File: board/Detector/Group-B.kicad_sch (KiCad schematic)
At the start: 27 parts, among them J2 Conn_02x04_Odd_Even, Q5 Q_Photo_NPN, Q6 Q_Photo_NPN, Q7 Q_Photo_NPN, Q8 Q_Photo_NPN, U2 LM339

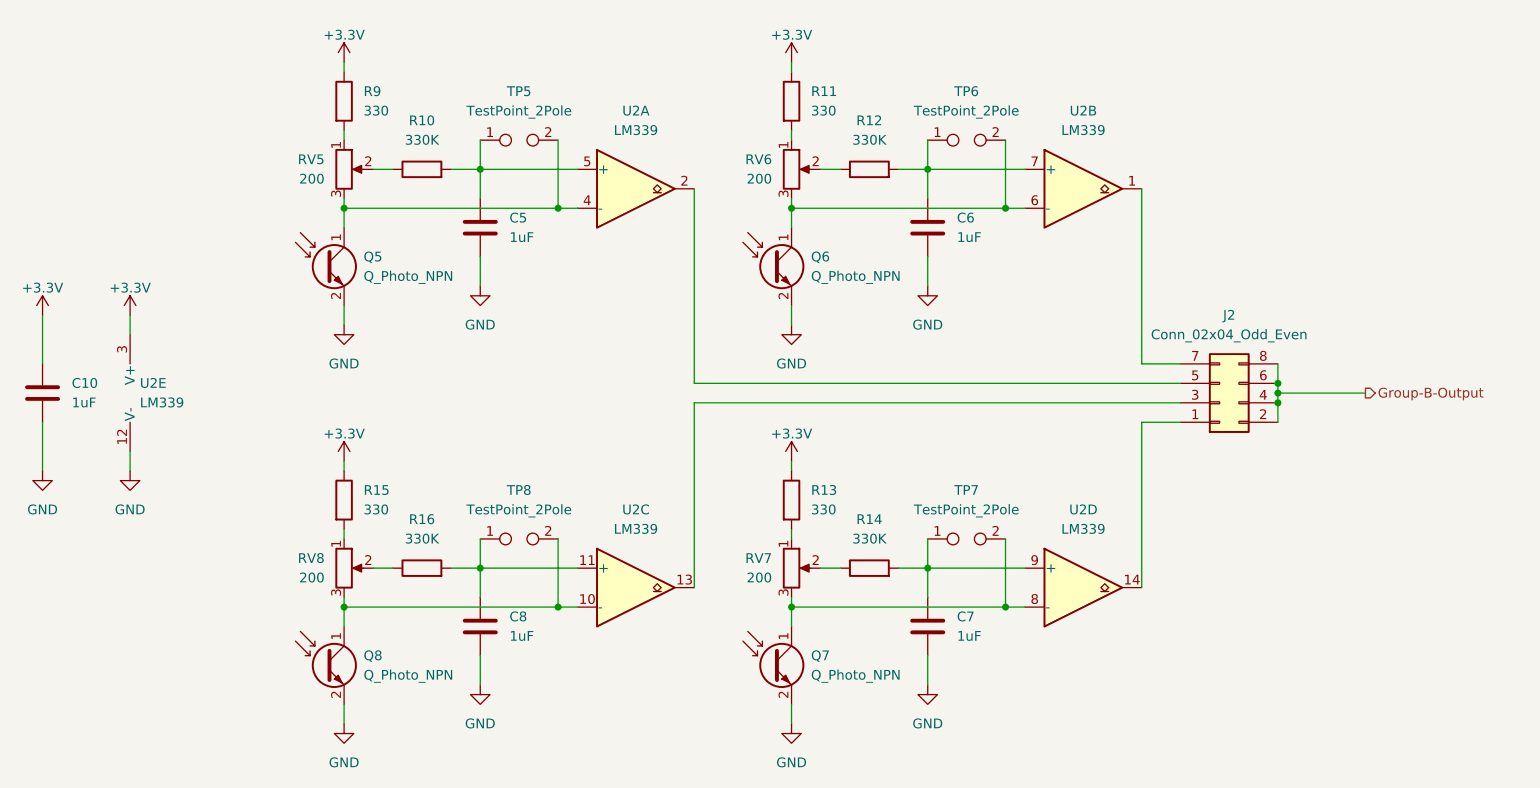
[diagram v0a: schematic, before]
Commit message: Fix the order of jumper links
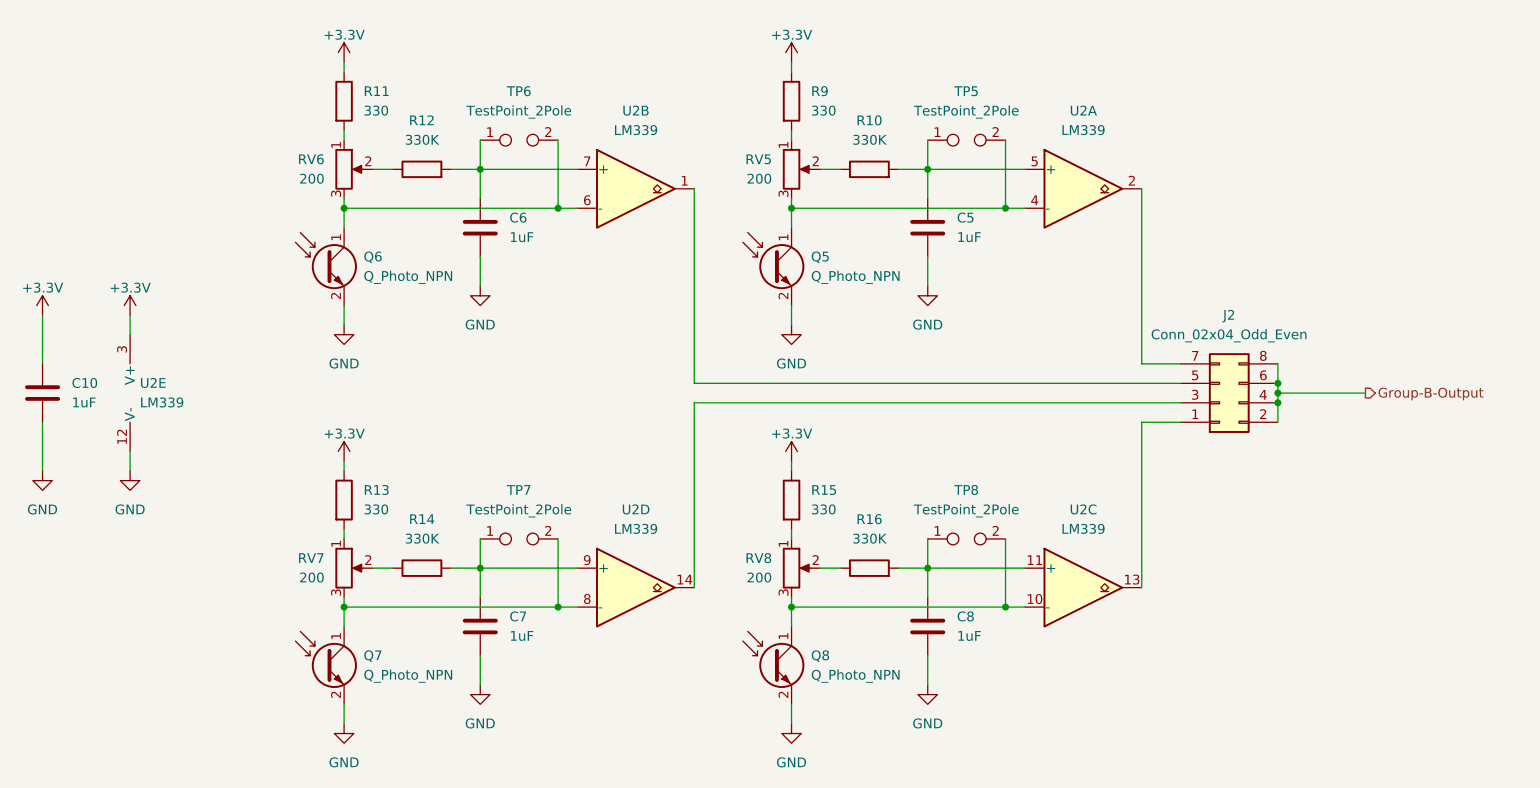
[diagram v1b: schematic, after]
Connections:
- net at U2.14: now also J2.3 (Pin_3); no longer J2.1 (Pin_1)
- net at U2.2: now also J2.7 (Pin_7); no longer J2.5 (Pin_5)
- net at U2.13: now also J2.1 (Pin_1); no longer J2.3 (Pin_3)
- net at U2.1: now also J2.5 (Pin_5); no longer J2.7 (Pin_7)
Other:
- moved on the sheet: C5, C6, C7, C8, Q5, Q6, Q7, Q8, R10, R11, R12, R13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

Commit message: Adjust values
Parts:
- Q5, Q6, Q7, Q8: value Q_Photo_NPN -> SFH 314 FA-2/3
- R11, R13, R15, R9: value 330 -> 2K
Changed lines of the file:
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@@
       (effects (font (size 1.27 1.27)) (justify left))
     )
-    (property "Value" "330" (id 1) (at 91.44 50.7999 0)
+    (property "Value" "2K" (id 1) (at 91.44 50.7999 0)
       (effects (font (size 1.27 1.27)) (justify left))
     )
@@
       (effects (font (size 1.27 1.27)) (justify left))
     )
-    (property "Value" "330" (id 1) (at 91.44 102.8699 0)
+    (property "Value" "2K" (id 1) (at 91.44 102.8699 0)
       (effects (font (size 1.27 1.27)) (justify left))
     )
@@
       (effects (font (size 1.27 1.27)) (justify left))
     )
-    (property "Value" "330" (id 1) (at 149.86 50.7999 0)
+    (property "Value" "2K" (id 1) (at 149.86 50.7999 0)
       (effects (font (size 1.27 1.27)) (justify left))
     )
@@
       (effects (font (size 1.27 1.27)) (justify left))
     )
-    (property "Value" "330" (id 1) (at 149.86 102.8699 0)
+    (property "Value" "2K" (id 1) (at 149.86 102.8699 0)
       (effects (font (size 1.27 1.27)) (justify left))
     )
@@
       (effects (font (size 1.27 1.27)) (justify left))
     )
-    (property "Value" "Q_Photo_NPN" (id 1) (at 91.44 72.3899 0)
+    (property "Value" "SFH 314 FA-2/3" (id 1) (at 91.44 72.3899 0)
       (effects (font (size 1.27 1.27)) (justify left))
     )
@@
       (effects (font (size 1.27 1.27)) (justify left))
     )
-    (property "Value" "Q_Photo_NPN" (id 1) (at 91.44 124.4599 0)
+    (property "Value" "SFH 314 FA-2/3" (id 1) (at 91.44 124.4599 0)
       (effects (font (size 1.27 1.27)) (justify left))
     )
@@
       (effects (font (size 1.27 1.27)) (justify left))
     )
-    (property "Value" "Q_Photo_NPN" (id 1) (at 149.86 72.3899 0)
+    (property "Value" "SFH 314 FA-2/3" (id 1) (at 149.86 72.3899 0)
       (effects (font (size 1.27 1.27)) (justify left))
     )
@@
       (effects (font (size 1.27 1.27)) (justify left))
     )
-    (property "Value" "Q_Photo_NPN" (id 1) (at 149.86 124.4599 0)
-      (effects (font (size 1.27 1.27)) (justify left))
-    )
+    (property "Value" "SFH 314 FA-2/3" (id 1) (at 149.86 124.4599 0)
+      (effects (font (size 1.27 1.27)) (justify left))
+    )

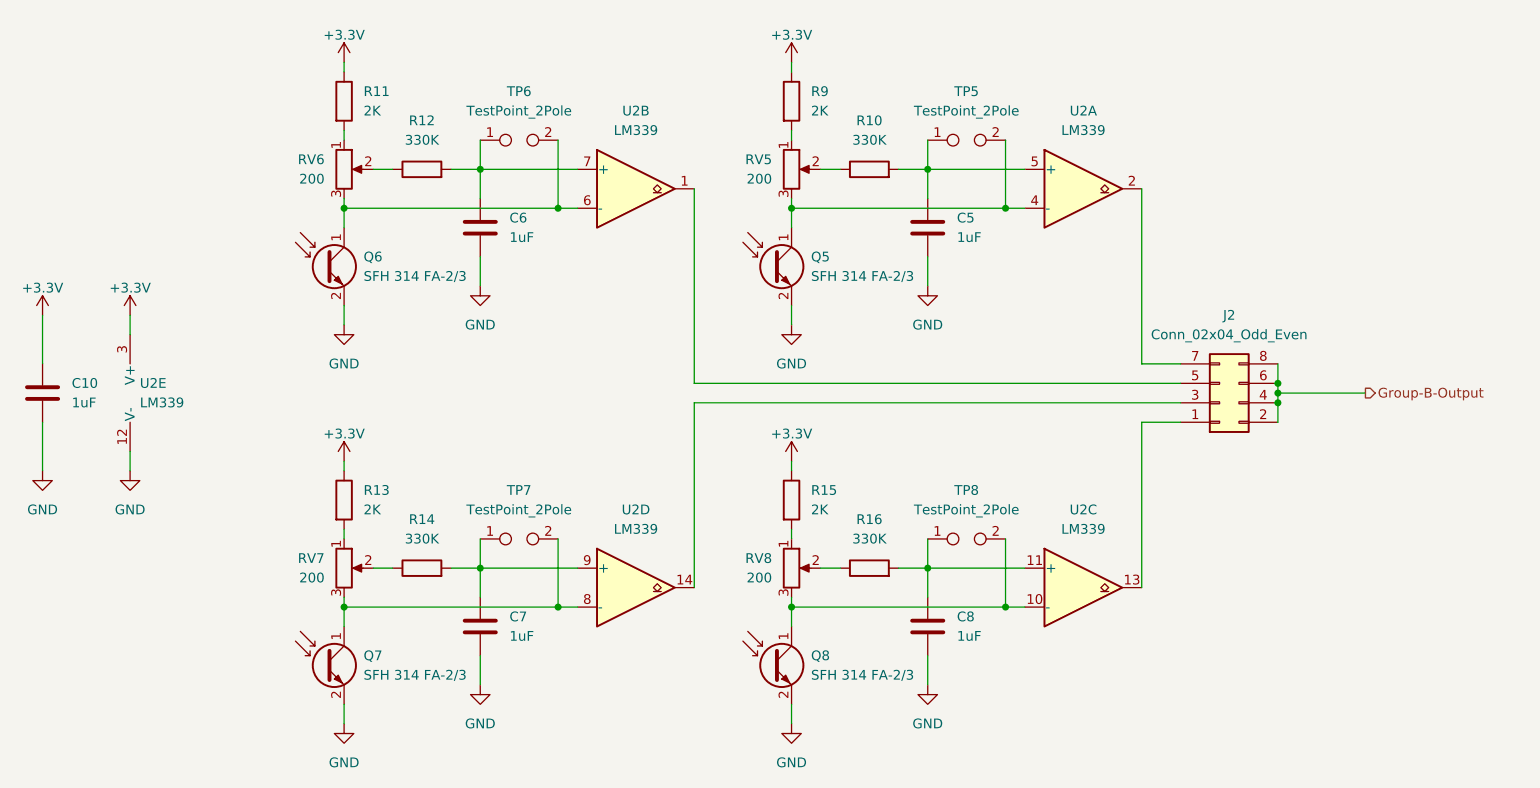
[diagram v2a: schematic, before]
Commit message: Detector changes to better control overall bias level
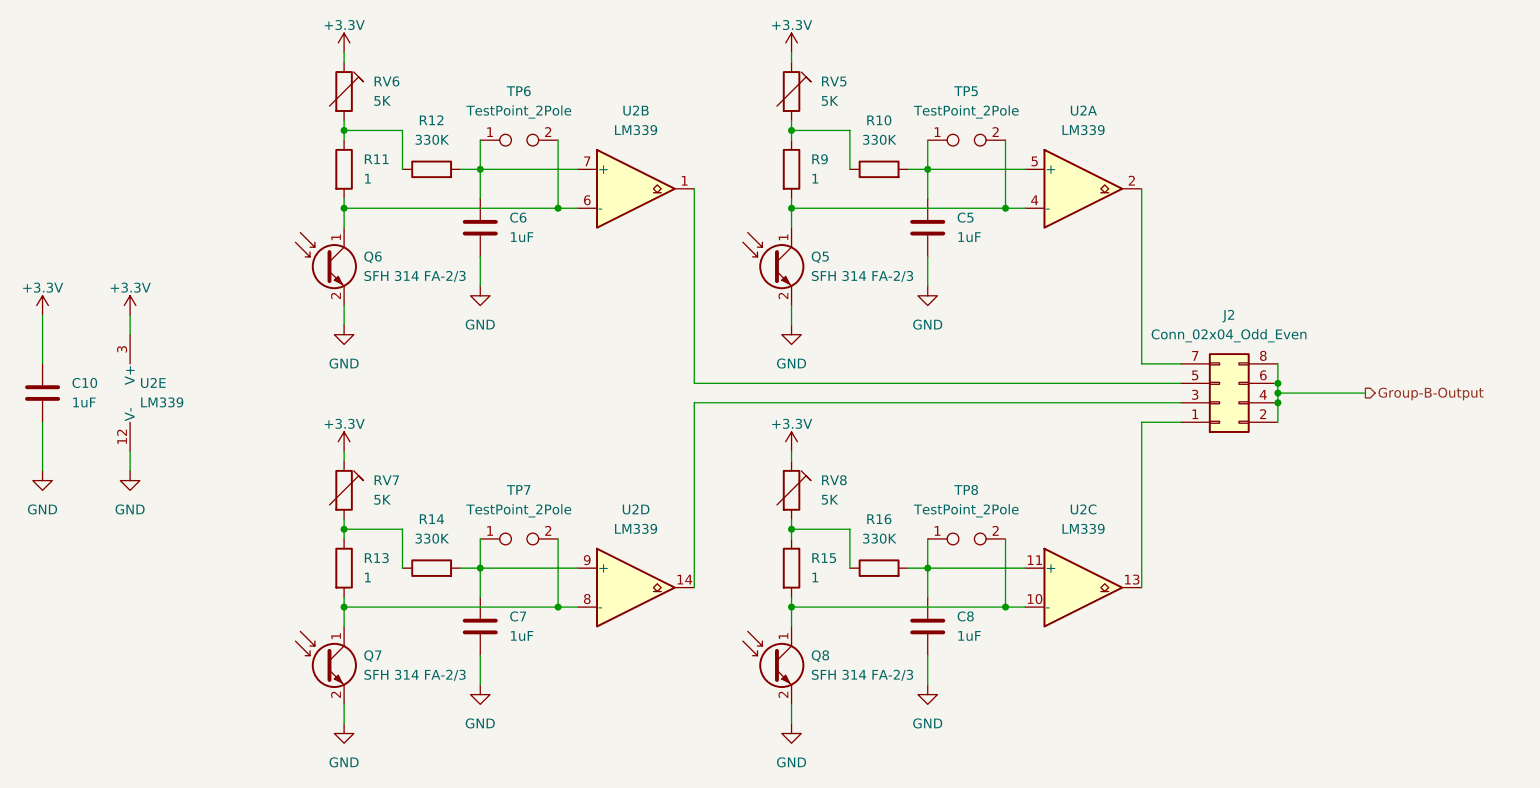
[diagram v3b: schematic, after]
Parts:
- removed RV5, RV6, RV7, RV8: 200, SamacSys_Parts:3362P_1, symbol Device:R_Potentiometer
- added RV5, RV6, RV7, RV8: 5K, SamacSys_Parts:3362P_1, symbol Device:R_Trim
- Q5, Q6, Q7, Q8: footprint LED_THT:LED_D3.0mm_Clear -> LED_THT:LED_D3.0mm_IRBlack
- R11, R13, R15, R9: value 2K -> 1
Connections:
- net +3V3: now also RV5.1, RV6.1, RV7.1, RV8.1; no longer R11.1, R13.1, R15.1, R9.1
- net at R14.1: now also R13.1, RV7.2
- net at Q7.1 (C), TP7.2, U2.8 (-): now also R13.2
- net at R15.2: now also Q8.1 (C), TP8.2, U2.10 (-)
- net at R16.1: now also R15.1, RV8.2
- net at Q5.1 (C), TP5.2, U2.4 (-): now also R9.2
- net at R11.2: now also Q6.1 (C), TP6.2, U2.6 (-)
- net at R12.1: now also R11.1, RV6.2
- net at R10.1: now also R9.1, RV5.2
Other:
- moved on the sheet: R10, R11, R12, R13, R14, R15, R16, R9

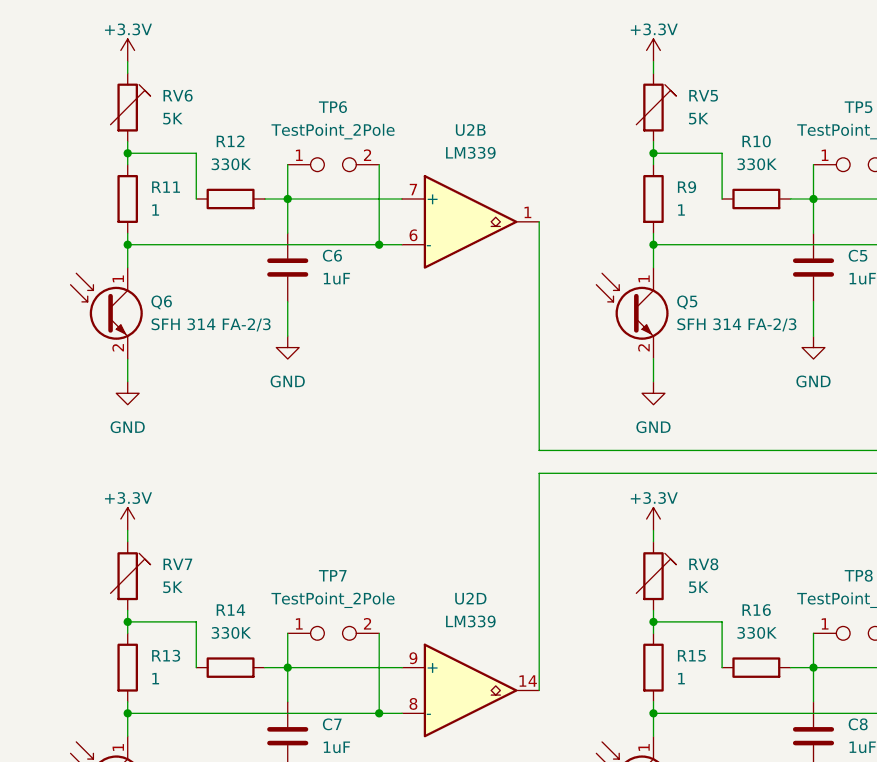
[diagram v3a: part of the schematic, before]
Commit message: Changed connectors, 3D models, added test points
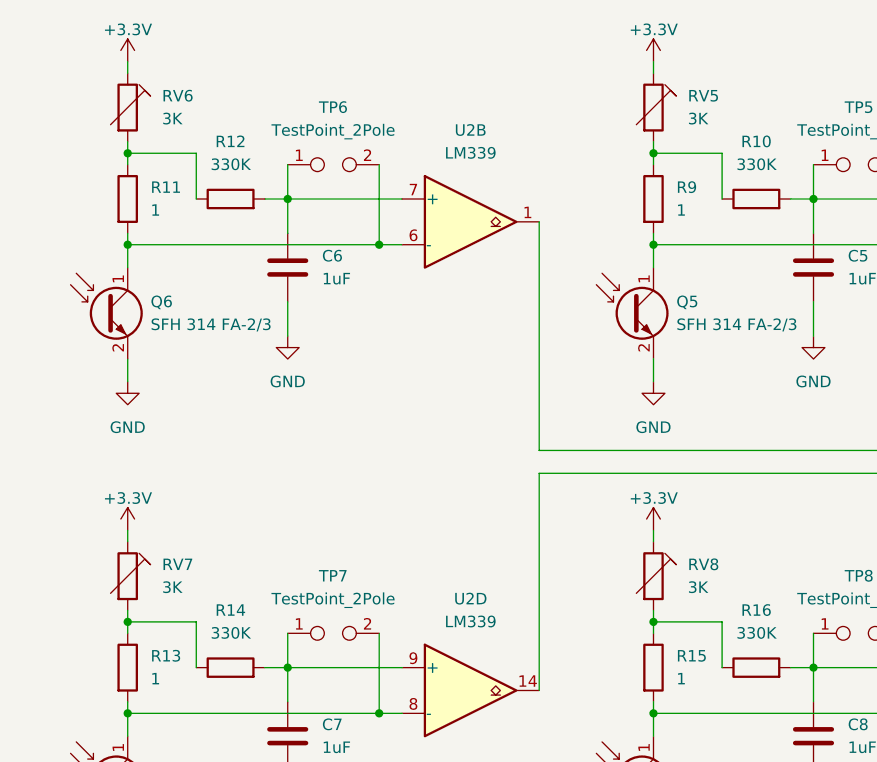
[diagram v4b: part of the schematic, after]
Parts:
- RV5, RV6, RV7, RV8: value 5K -> 3K

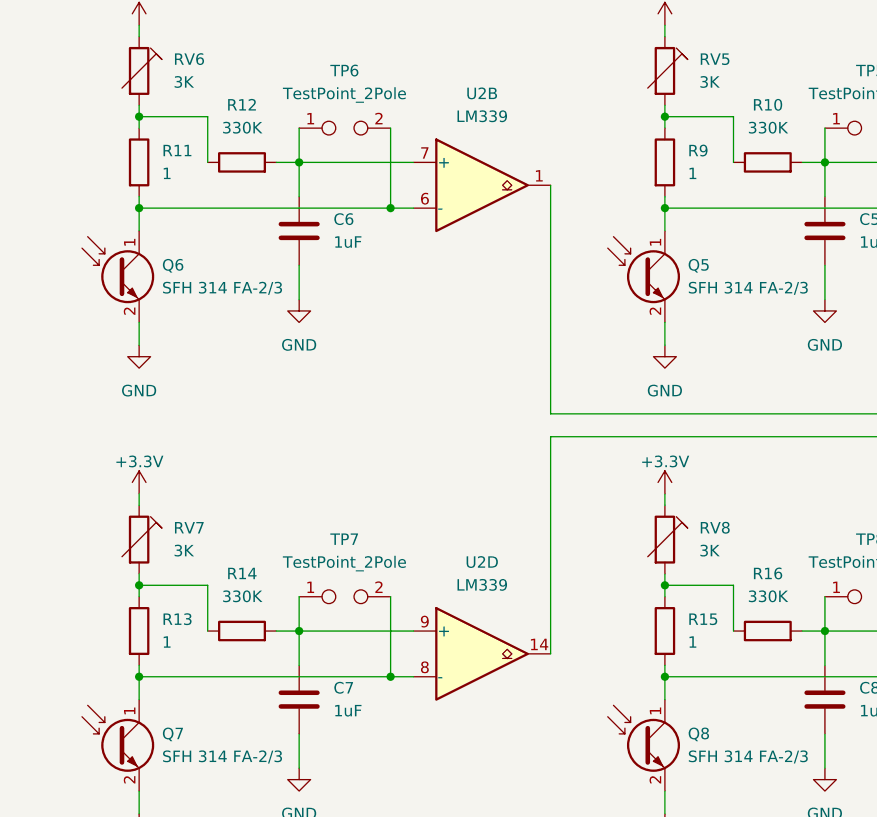
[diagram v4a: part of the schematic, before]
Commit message: Reduce sensitivity so we don't trigger on dust
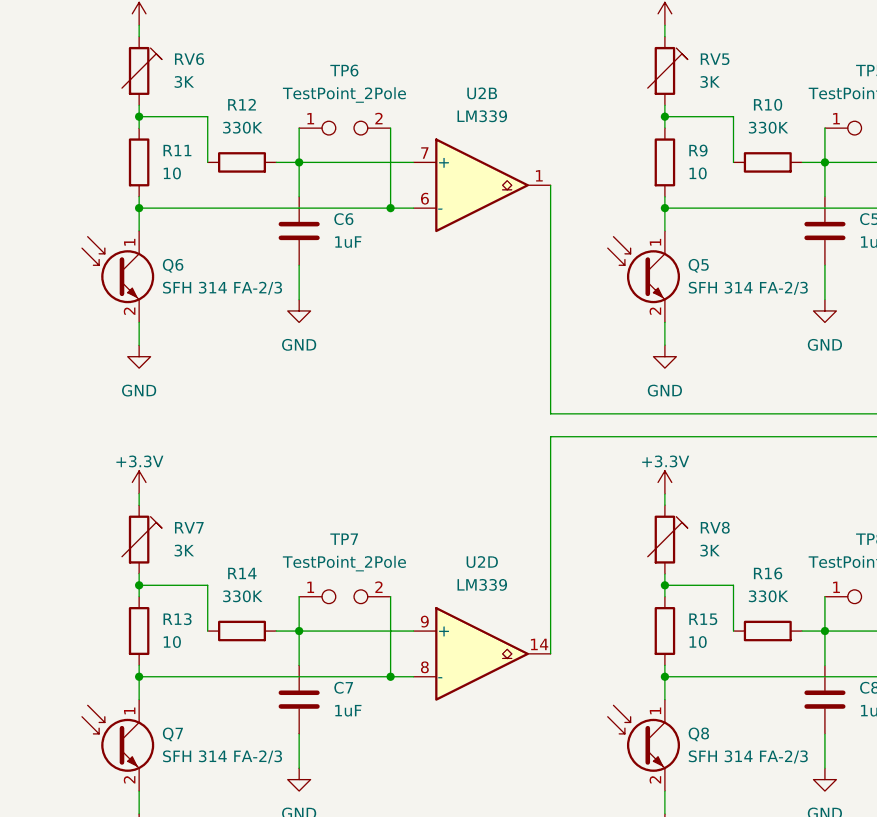
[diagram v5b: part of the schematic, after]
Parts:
- R11, R13, R15, R9: value 1 -> 10
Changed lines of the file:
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@@
       (effects (font (size 1.27 1.27)) hide)
     )
+    (pin "2")
+    (pin "4")
+    (pin "5")
+    (pin "1")
+    (pin "6")
+    (pin "7")
+    (pin "10")
+    (pin "11")
+    (pin "13")
     (pin "14")
     (pin "8")
     (pin "9")
+    (pin "12")
+    (pin "3")
   )
   (symbol (lib_id "power:GND") (at 106.68 73.66 0) (unit 1)
@@
       (effects (font (size 1.27 1.27)) hide)
     )
+    (pin "2")
+    (pin "4")
+    (pin "5")
+    (pin "1")
+    (pin "6")
+    (pin "7")
+    (pin "10")
+    (pin "11")
+    (pin "13")
+    (pin "14")
+    (pin "8")
+    (pin "9")
     (pin "12")
     (pin "3")
@@
       (effects (font (size 1.27 1.27)) (justify left))
     )
-    (property "Value" "1" (id 1) (at 91.44 59.6899 0)
+    (property "Value" "10" (id 1) (at 91.44 59.6899 0)
       (effects (font (size 1.27 1.27)) (justify left))
     )
@@
       (effects (font (size 1.27 1.27)) (justify left))
     )
-    (property "Value" "1" (id 1) (at 149.86 111.7599 0)
+    (property "Value" "10" (id 1) (at 149.86 111.7599 0)
       (effects (font (size 1.27 1.27)) (justify left))
     )
@@
     (pin "4")
     (pin "5")
+    (pin "1")
+    (pin "6")
+    (pin "7")
+    (pin "10")
+    (pin "11")
+    (pin "13")
+    (pin "14")
+    (pin "8")
+    (pin "9")
+    (pin "12")
+    (pin "3")
   )
   (symbol (lib_id "power:GND") (at 49.53 97.79 0) (unit 1)
@@
       (effects (font (size 1.27 1.27)) (justify left))
     )
-    (property "Value" "1" (id 1) (at 149.86 59.6899 0)
+    (property "Value" "10" (id 1) (at 149.86 59.6899 0)
       (effects (font (size 1.27 1.27)) (justify left))
     )
@@
       (effects (font (size 1.27 1.27)) (justify left))
     )
-    (property "Value" "1" (id 1) (at 91.44 111.7599 0)
+    (property "Value" "10" (id 1) (at 91.44 111.7599 0)
       (effects (font (size 1.27 1.27)) (justify left))
     )
@@
       (effects (font (size 1.27 1.27)) hide)
     )
+    (pin "2")
+    (pin "4")
+    (pin "5")
+    (pin "1")
+    (pin "6")
+    (pin "7")
     (pin "10")
     (pin "11")
     (pin "13")
+    (pin "14")
+    (pin "8")
+    (pin "9")
+    (pin "12")
+    (pin "3")
   )
   (symbol (lib_id "Device:R_Trim") (at 88.9 100.33 0) (unit 1)
@@
       (effects (font (size 1.27 1.27)) hide)
     )
+    (pin "2")
+    (pin "4")
+    (pin "5")
     (pin "1")
     (pin "6")
     (pin "7")
+    (pin "10")
+    (pin "11")
+    (pin "13")
+    (pin "14")
+    (pin "8")
+    (pin "9")
+    (pin "12")
+    (pin "3")
   )
   (symbol (lib_id "Connector:TestPoint_2Pole") (at 170.18 106.68 0) (unit 1)
